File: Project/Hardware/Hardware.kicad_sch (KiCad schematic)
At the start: 13 parts, among them U1 LCD1602_I2C, U2 HM-10, U3 DS3231M

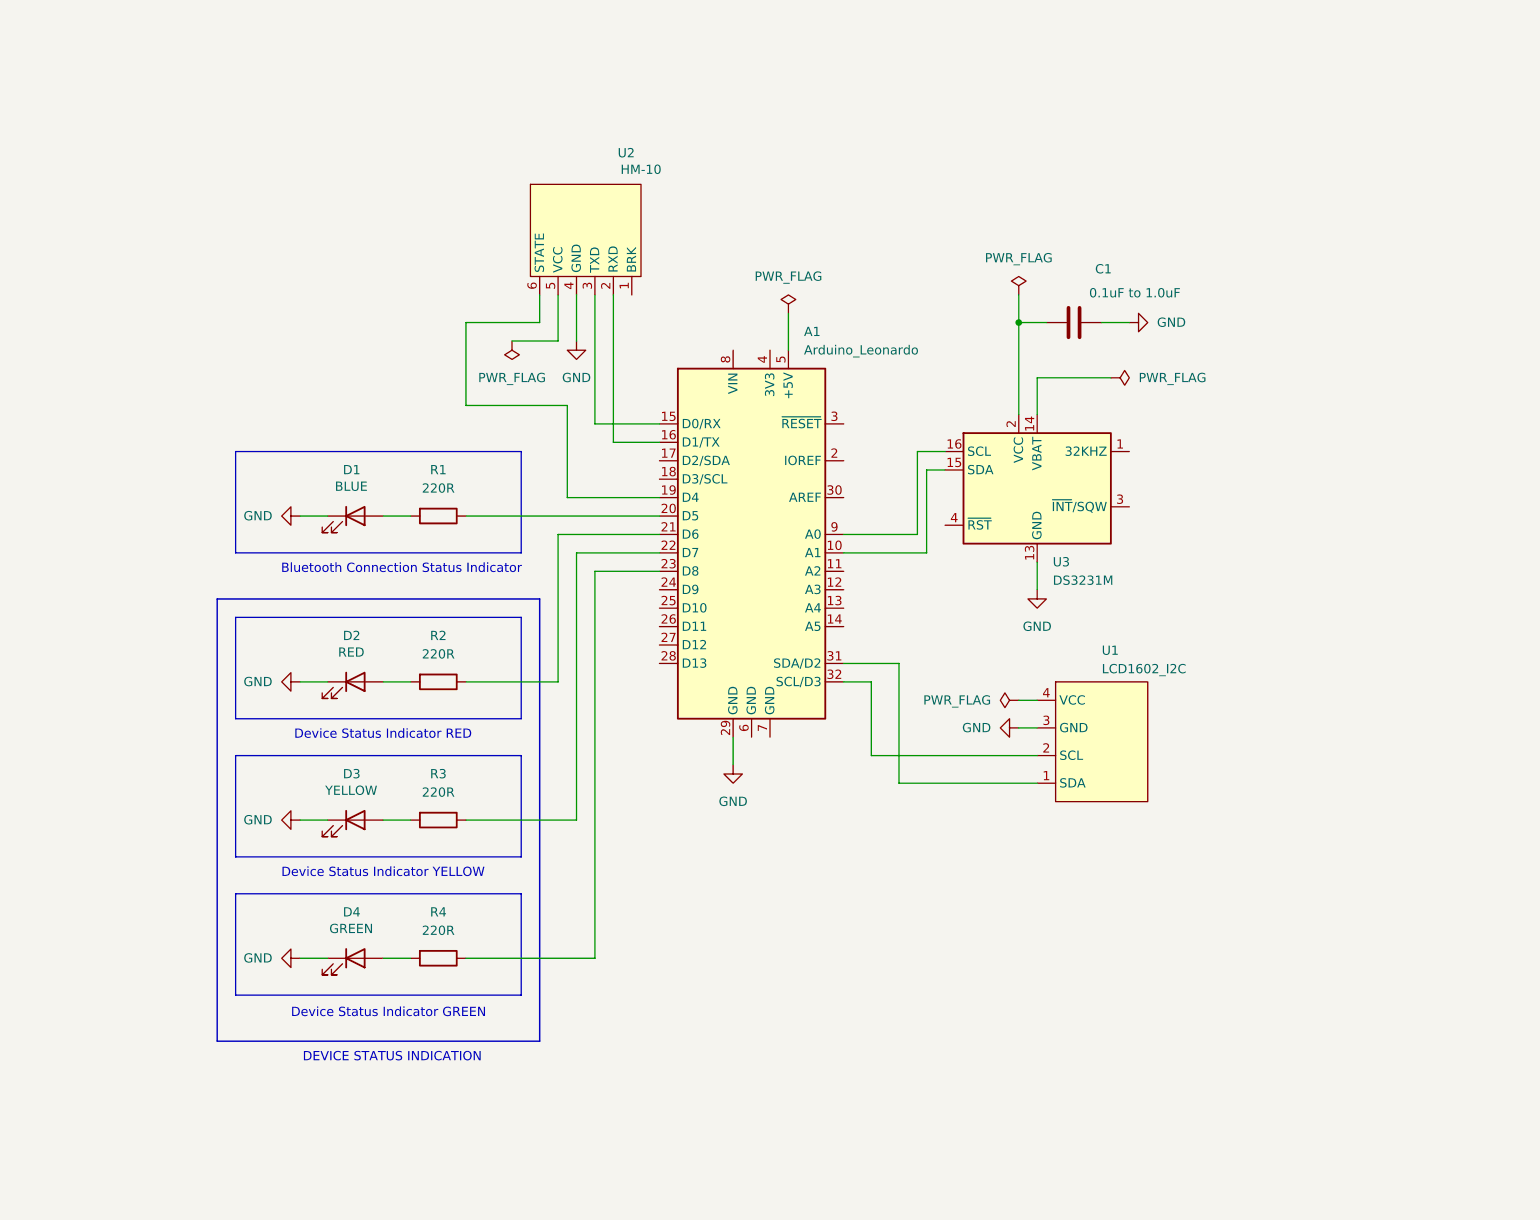
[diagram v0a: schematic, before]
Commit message: Reorganise schematic and add buttons
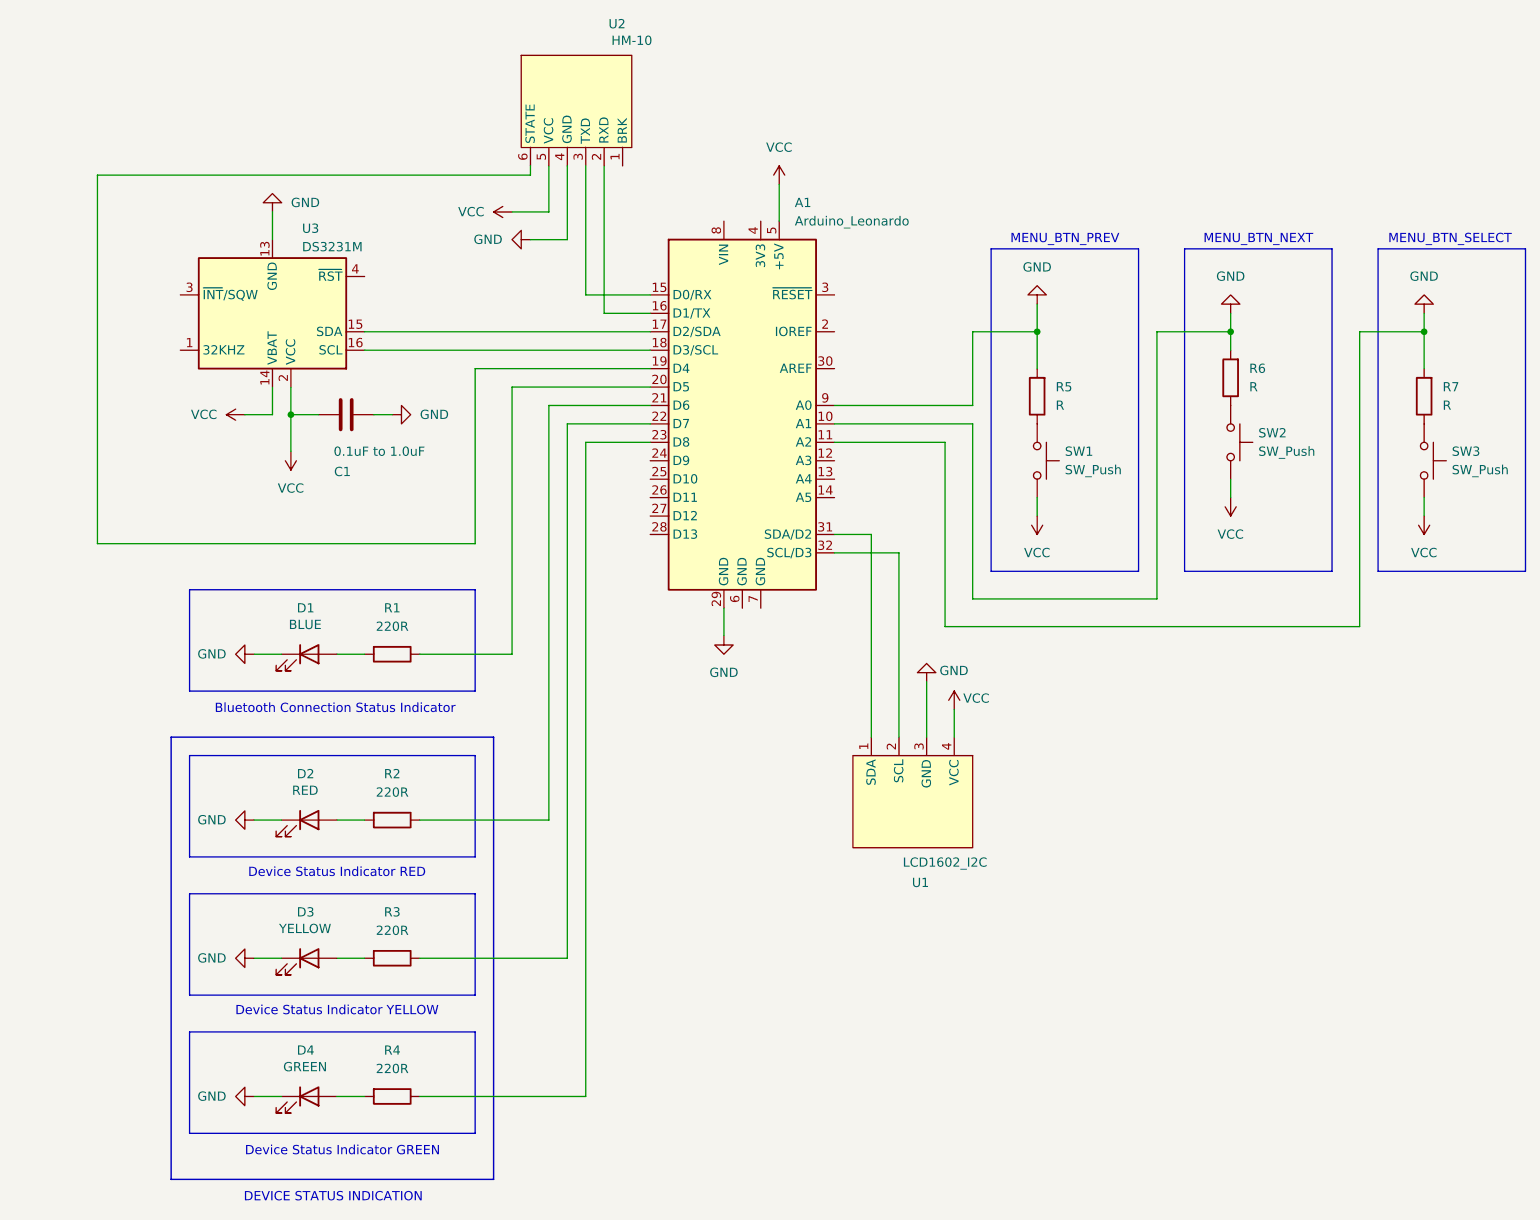
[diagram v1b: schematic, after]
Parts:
- added R5, R6, R7: R, symbol Device:R
- added SW1, SW2, SW3: SW_Push, symbol Switch:SW_Push
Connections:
- net GND: now also A1.10 (A1), A1.11 (A2), A1.9 (A0), C1.2, R5.2, R6.2, R7.2; no longer C1.1
- net VCC: now reaches U1.4 (VCC)
- net VCC: now also A1.5 (+5V), C1.1, U2.5 (VCC), U3.14 (VBAT), U3.2 (VCC), SW1.2, SW2.2, SW3.2
- net at U3.15 (SDA): now also A1.17 (D2/SDA); no longer A1.10 (A1)
- net at U3.16 (SCL): now also A1.18 (D3/SCL); no longer A1.9 (A0)
- new net: R6.1, SW2.1
- new net: R5.1, SW1.1
- new net: R7.1, SW3.1
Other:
- note added: "MENU_BTN_NEXT"
- note added: "MENU_BTN_PREV"
- note added: "MENU_BTN_SELECT"
- moved on the sheet: A1, C1, D1, D2, D3, D4, R1, R2, R3, R4, U1, U2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

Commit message: Edit resistance values in schematic
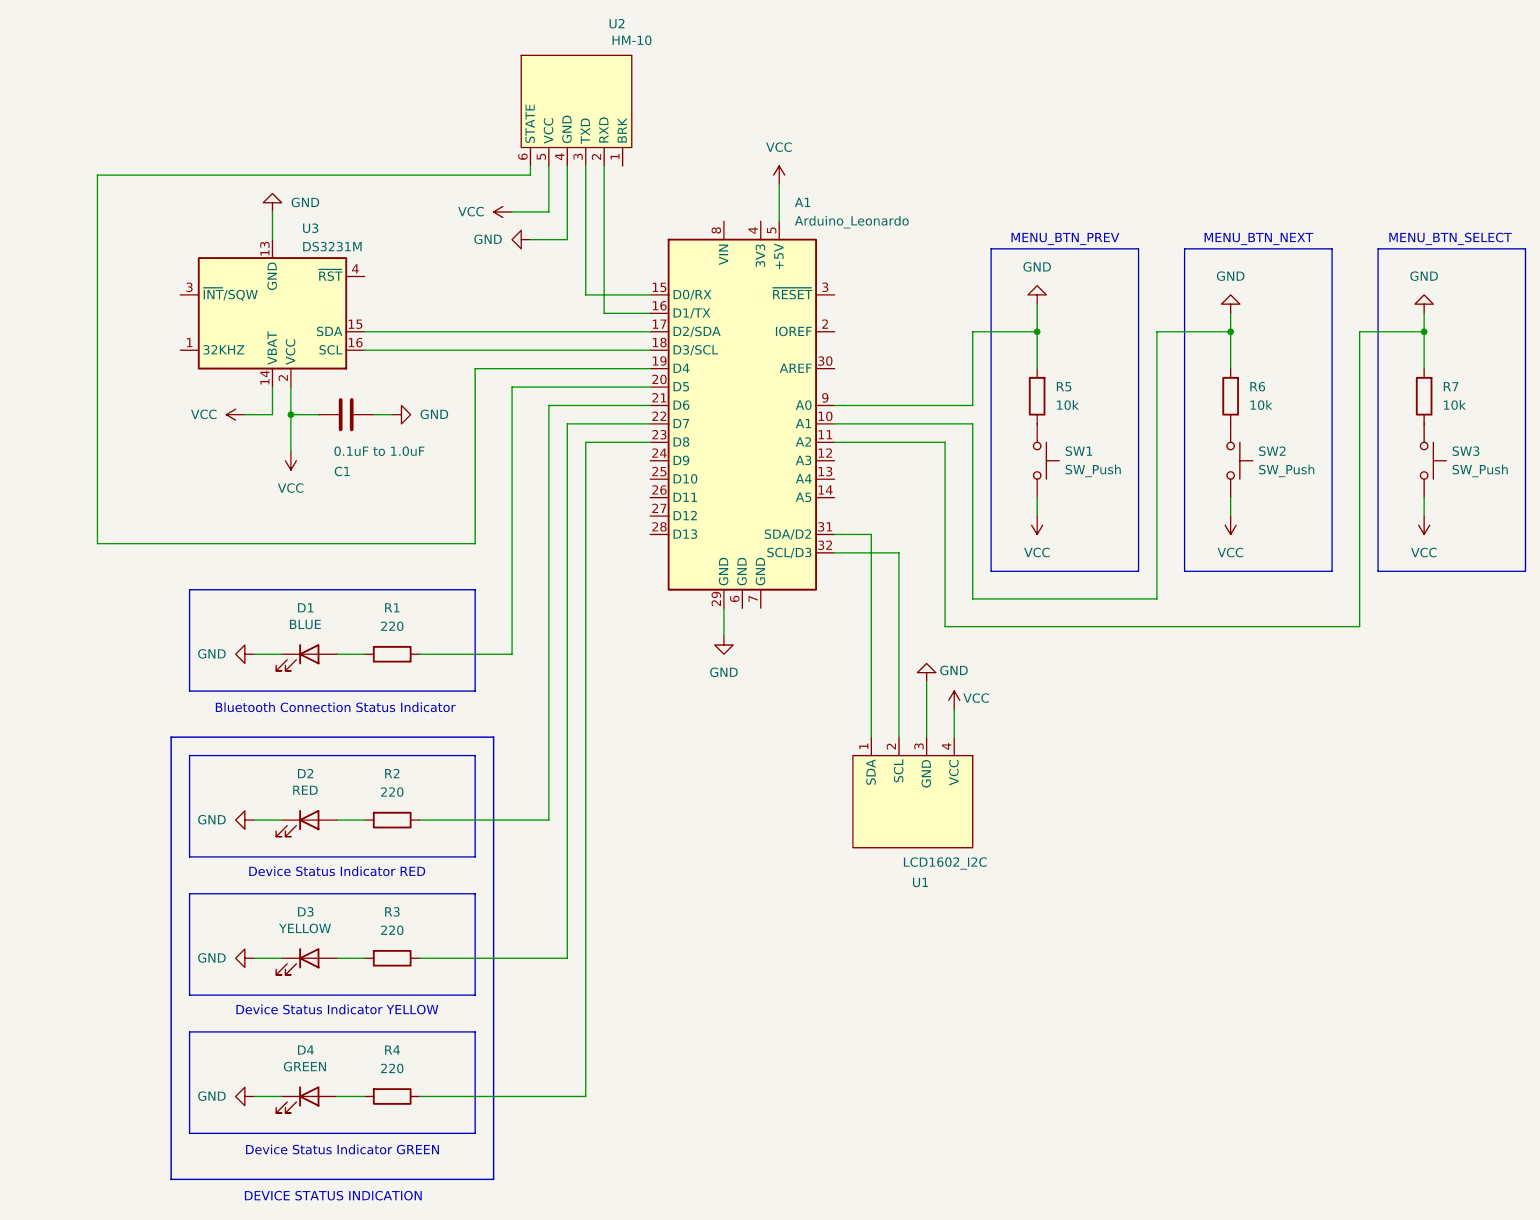
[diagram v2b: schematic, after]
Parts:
- R1, R2, R3, R4: value 220R -> 220
- R5, R6, R7: value R -> 10k
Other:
- moved on the sheet: R6, SW2
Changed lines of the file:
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@@
 	(title_block
 		(title "Traffic Modeling and Traffic Analysis for LoRaWAN Networks")
-		(date "2025-04-14")
+		(date "2025-04-15")
 		(rev "2")
 		(comment 2 "Author: Martin Aziz")
@@
 	(wire
 		(pts
-			(xy 218.44 87.63) (xy 218.44 90.17)
+			(xy 218.44 90.17) (xy 218.44 92.71)
 		)
 		(stroke
@@
 	(wire
 		(pts
-			(xy 218.44 67.31) (xy 218.44 69.85)
+			(xy 218.44 67.31) (xy 218.44 72.39)
 		)
 		(stroke
@@
 	(symbol
 		(lib_id "Device:R")
-		(at 218.44 73.66 180)
+		(at 218.44 76.2 180)
 		(unit 1)
 		(exclude_from_sim no)
@@
 		(fields_autoplaced yes)
 		(property "Reference" "R6"
-			(at 220.98 72.3899 0)
+			(at 220.98 74.9299 0)
 			(effects
 				(font
@@
 			)
 		)
-		(property "Value" "R"
-			(at 220.98 74.9299 0)
+		(property "Value" "10k"
+			(at 220.98 77.4699 0)
 			(effects
 				(font
@@
 		)
 		(property "Footprint" ""
-			(at 220.218 73.66 90)
+			(at 220.218 76.2 90)
 			(effects
 				(font
@@
 		)
 		(property "Datasheet" "~"
-			(at 218.44 73.66 0)
+			(at 218.44 76.2 0)
 			(effects
 				(font
@@
 		)
 		(property "Description" "Resistor"
-			(at 218.44 73.66 0)
+			(at 218.44 76.2 0)
 			(effects
 				(font
@@
 			)
 		)
-		(property "Value" "220R"
+		(property "Value" "220"
 			(at 102.87 168.91 90)
 			(effects
@@
 			)
 		)
-		(property "Value" "R"
+		(property "Value" "10k"
 			(at 247.65 77.4699 0)
 			(effects
@@
 			)
 		)
-		(property "Value" "220R"
+		(property "Value" "220"
 			(at 102.87 130.81 90)
 			(effects
@@
 			)
 		)
-		(property "Value" "R"
+		(property "Value" "10k"
 			(at 194.31 77.4699 0)
 			(effects
@@
 			)
 		)
-		(property "Value" "220R"
+		(property "Value" "220"
 			(at 102.87 149.86 90)
 			(effects
@@
 	(symbol
 		(lib_id "power:VCC")
-		(at 218.44 90.17 180)
+		(at 218.44 92.71 180)
 		(unit 1)
 		(exclude_from_sim no)
@@
 		(fields_autoplaced yes)
 		(property "Reference" "#PWR014"
-			(at 218.44 86.36 0)
+			(at 218.44 88.9 0)
 			(effects
 				(font
@@
 		)
 		(property "Value" "VCC"
-			(at 218.44 95.25 0)
+			(at 218.44 97.79 0)
 			(effects
 				(font
@@
 		)
 		(property "Footprint" ""
-			(at 218.44 90.17 0)
+			(at 218.44 92.71 0)
 			(effects
 				(font
@@
 		)
 		(property "Datasheet" ""
-			(at 218.44 90.17 0)
+			(at 218.44 92.71 0)
 			(effects
 				(font
@@
 		)
 		(property "Description" "Power symbol creates a global label with name \"VCC\""
-			(at 218.44 90.17 0)
+			(at 218.44 92.71 0)
 			(effects
 				(font
@@
 			)
 		)
-		(property "Value" "220R"
+		(property "Value" "220"
 			(at 102.87 107.95 90)
 			(effects
@@
 	(symbol
 		(lib_id "Switch:SW_Push")
-		(at 218.44 82.55 270)
+		(at 218.44 85.09 270)
 		(unit 1)
 		(exclude_from_sim no)
@@
 		(fields_autoplaced yes)
 		(property "Reference" "SW2"
-			(at 222.25 81.2799 90)
+			(at 222.25 83.8199 90)
 			(effects
 				(font
@@
 		)
 		(property "Value" "SW_Push"
-			(at 222.25 83.8199 90)
+			(at 222.25 86.3599 90)
 			(effects
 				(font
@@
 		)
 		(property "Footprint" ""
-			(at 223.52 82.55 0)
+			(at 223.52 85.09 0)
 			(effects
 				(font
@@
 		)
 		(property "Datasheet" "~"
-			(at 223.52 82.55 0)
+			(at 223.52 85.09 0)
 			(effects
 				(font
@@
 		)
 		(property "Description" "Push button switch, generic, two pins"
-			(at 218.44 82.55 0)
+			(at 218.44 85.09 0)
 			(effects
 				(font

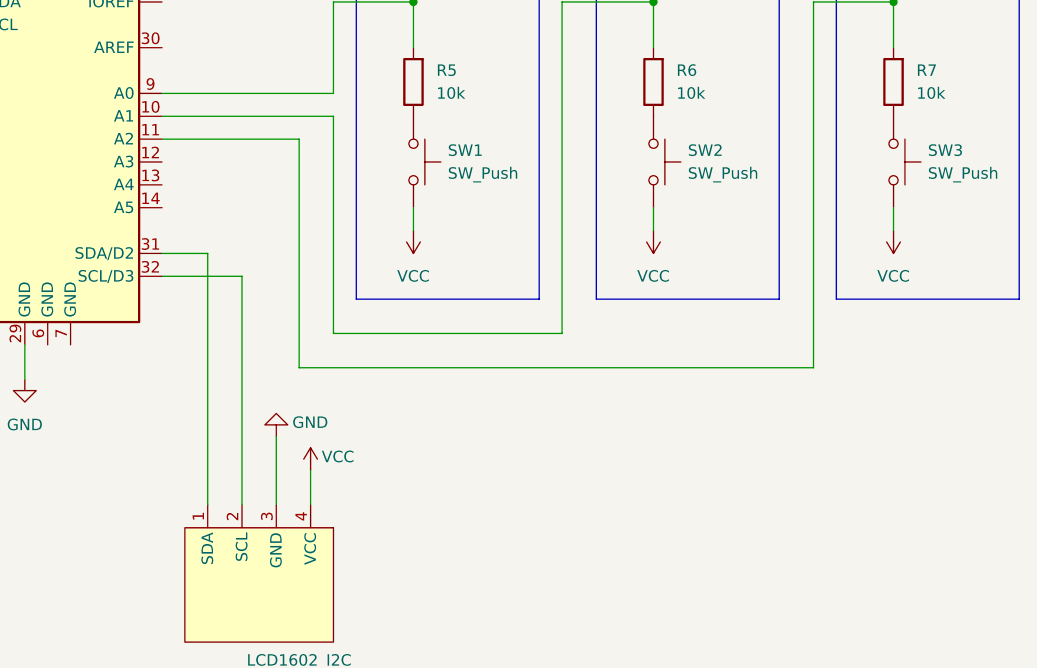
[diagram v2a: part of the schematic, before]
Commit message: Add buzzer
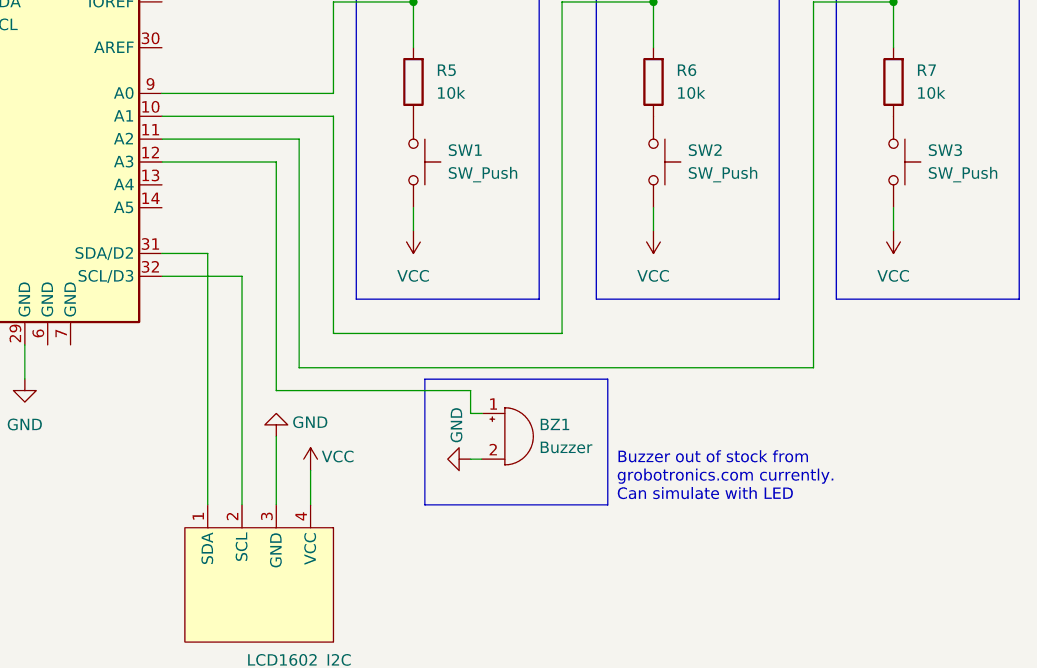
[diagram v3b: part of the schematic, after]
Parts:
- added BZ1: Buzzer, symbol Device:Buzzer
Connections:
- net GND: now also BZ1.2 (-)
- net at A1.12 (A3): now also BZ1.1 (+)
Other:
- note added: "Buzzer out of stock from grobotronics.com currently. Can simulate with LED"
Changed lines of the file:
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@@
+	)
+	(rectangle
+		(start 193.04 109.22)
+		(end 213.36 123.19)
+		(stroke
+			(width 0)
+			(type default)
+		)
+		(fill
+			(type none)
+		)
 	)
 	(rectangle
@@
 		)
 	)
+	(text "Buzzer out of stock from\ngrobotronics.com currently.\nCan simulate with LED"
+		(exclude_from_sim no)
+		(at 214.376 120.142 0)
+		(effects
+			(font
+				(size 1.27 1.27)
+			)
+			(justify left)
+		)
+	)
 	(text "MENU_BTN_SELECT"
 		(exclude_from_sim no)
@@
 	(wire
 		(pts
+			(xy 176.53 110.49) (xy 198.12 110.49)
+		)
+		(stroke
+			(width 0)
+			(type default)
+		)
+	)
+	(wire
+		(pts
 			(xy 208.28 67.31) (xy 218.44 67.31)
 		)
@@
 	(wire
 		(pts
+			(xy 176.53 110.49) (xy 176.53 85.09)
+		)
+		(stroke
+			(width 0)
+			(type default)
+		)
+	)
+	(wire
+		(pts
 			(xy 132.08 64.77) (xy 138.43 64.77)
 		)
@@
 	(wire
 		(pts
+			(xy 198.12 110.49) (xy 198.12 113.03)
+		)
+		(stroke
+			(width 0)
+			(type default)
+		)
+	)
+	(wire
+		(pts
 			(xy 95.25 172.72) (xy 99.06 172.72)
 		)
@@
 	(wire
 		(pts
+			(xy 198.12 113.03) (xy 199.39 113.03)
+		)
+		(stroke
+			(width 0)
+			(type default)
+		)
+	)
+	(wire
+		(pts
 			(xy 100.33 78.74) (xy 102.87 78.74)
 		)
@@
 	(wire
 		(pts
+			(xy 198.12 118.11) (xy 199.39 118.11)
+		)
+		(stroke
+			(width 0)
+			(type default)
+		)
+	)
+	(wire
+		(pts
 			(xy 121.92 54.61) (xy 127 54.61)
 		)
@@
 		(pts
 			(xy 172.72 97.79) (xy 172.72 123.19)
+		)
+		(stroke
+			(width 0)
+			(type default)
+		)
+	)
+	(wire
+		(pts
+			(xy 176.53 85.09) (xy 163.83 85.09)
 		)
 		(stroke
@@
 					(unit 1)
 				)
+			)
+		)
+	)
+	(symbol
+		(lib_id "power:GND")
+		(at 198.12 118.11 270)
+		(unit 1)
+		(exclude_from_sim no)
+		(in_bom yes)
+		(on_board yes)
+		(dnp no)
+		(property "Reference" "#PWR021"
+			(at 191.77 118.11 0)
+			(effects
+				(font
+					(size 1.27 1.27)
+				)
+				(hide yes)
+			)
+		)
+		(property "Value" "GND"
+			(at 196.596 116.332 0)
+			(effects
+				(font
+					(size 1.27 1.27)
+				)
+				(justify right)
+			)
+		)
+		(property "Footprint" ""
+			(at 198.12 118.11 0)
+			(effects
+				(font
+					(size 1.27 1.27)
+				)
+				(hide yes)
+			)
+		)
+		(property "Datasheet" ""
+			(at 198.12 118.11 0)
+			(effects
+				(font
+					(size 1.27 1.27)
+				)
+				(hide yes)
+			)
+		)
+		(property "Description" "Power symbol creates a global label with name \"GND\" , ground"
+			(at 198.12 118.11 0)
+			(effects
+				(font
+					(size 1.27 1.27)
+				)
+				(hide yes)
+			)
+		)
+		(pin "1"
+		)
+		(instances
+			(project "Hardware"
+				(path "/823843db-cbc4-413a-a2ac-ffbd107e023e"
+					(reference "#PWR021")
+					(unit 1)
+				)
+			)
+		)
+	)
+	(symbol
+		(lib_id "Device:Buzzer")
+		(at 201.93 115.57 0)
+		(unit 1)
+		(exclude_from_sim no)
+		(in_bom yes)
+		(on_board yes)
+		(dnp no)
+		(fields_autoplaced yes)
+		(property "Reference" "BZ1"
+			(at 205.74 114.2999 0)
+			(effects
+				(font
+					(size 1.27 1.27)
+				)
+				(justify left)
+			)
+		)
+		(property "Value" "Buzzer"
+			(at 205.74 116.8399 0)
+			(effects
+				(font
+					(size 1.27 1.27)
+				)
+				(justify left)
+			)
+		)
+		(property "Footprint" ""
+			(at 201.295 113.03 90)
+			(effects
+				(font
+					(size 1.27 1.27)
+				)
+				(hide yes)
+			)
+		)
+		(property "Datasheet" "~"
+			(at 201.295 113.03 90)
+			(effects
+				(font
+					(size 1.27 1.27)
+				)
+				(hide yes)
+			)
+		)
+		(property "Description" "Buzzer, polarized"
+			(at 201.93 115.57 0)
+			(effects
+				(font
+					(size 1.27 1.27)
+				)
+				(hide yes)
+			)
+		)
+		(pin "1"
+		)
+		(pin "2"
+		)
+		(instances
+			(project ""
+				(path "/823843db-cbc4-413a-a2ac-ffbd107e023e"
+					(reference "BZ1")
+					(unit 1)
+				)
